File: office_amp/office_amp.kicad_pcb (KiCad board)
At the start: 4 copper layers, 120 x 100 mm, 88 parts, among them J1 Jack-DC, J2 Conn_01x03_Female, J3 Conn_01x02_Female, J4 Conn_01x02_Female, J5 Conn_01x02_Female, J6 Conn_01x02_Female, J7 Screw_Terminal_01x04, K1 EC2-24NU, K2 EC2-24NU, K3 EC2-24NU, K4 EC2-24NU, Q1 DMT6012LSS, Q2 BC858, Q3 BC858, SW1 SW_SP3T, U1 LM74700, U2 TBA_2-2421, U3 OPA1678, U4 TBA_2-2421, U5 MH-M18, U6 TPA3123D2, U7 OPA1678, U8 IL300, U9 IL300

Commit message: zwischenstand
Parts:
- removed JP3, JP4: Jumper_2_Open, Jumper:SolderJumper-2_P1.3mm_Open_TrianglePad1.0x1.5mm
- added J8: Conn_01x03_Female, Connector_PinHeader_2.54mm:PinHeader_1x03_P2.54mm_Vertical, F.Cu at (174.0, 48.3)
- moved D1 258.2 mm to (203.0, 40.0)
- moved C29 253.8 mm to (203.5, 77.1), turned to 270 degrees
- moved C26 252.9 mm to (202.4, 83.1), turned to 0 degrees
- moved C27 250.9 mm to (202.4, 71.0), turned to 0 degrees
- moved R5 245.1 mm to (198.5, 83.1), turned to 0 degrees
- moved R6 243.1 mm to (198.5, 71.0), turned to 0 degrees
- moved U3 242.8 mm to (198.0, 77.1), turned to 90 degrees
- moved K4 242.3 mm to (180.3, 43.2)
- moved D4 237.3 mm to (193.0, 40.0)
- moved C30 236.0 mm to (194.0, 82.2), turned to 270 degrees
- moved K1 235.4 mm to (200.7, 43.2)
- moved K2 234.5 mm to (190.5, 43.2)
- moved C31 234.2 mm to (194.0, 72.0), turned to 270 degrees
- moved D6 233.0 mm to (182.9, 40.0)
- moved R7 232.0 mm to (192.0, 82.2), turned to 270 degrees
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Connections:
- C28 pad 2: GND_BT -> GND_Input
- C29 pad 1: GND_BT -> GND_Input
- C6 pad 2: PGND -> GNDREF
- C7 pad 2: GND_BT -> GND_Input
- C9 pad 1: GND_BT -> GND_Input
- D1 pad 1: V+ -> Net-(D1-Pad1)
- D1 pad 2: Net-(D1-Pad2) -> GNDREF
- D4 pad 1: V+ -> Net-(D1-Pad1)
- D4 pad 2: Net-(D4-Pad2) -> GNDREF
- D5 pad 1: V+ -> Net-(D5-Pad1)
- D5 pad 2: Net-(D5-Pad2) -> GNDREF
- D6 pad 1: V+ -> Net-(D5-Pad1)
- D6 pad 2: Net-(D6-Pad2) -> GNDREF
- J2 pad 1: (no net) -> GND_An_In
- K1 pad 1: Net-(K1-Pad1) -> Net-(D1-Pad1)
- K1 pad 10: (no net) -> L-In-USB
- K1 pad 12: Net-(D1-Pad2) -> GNDREF
- K1 pad 3: (no net) -> R-In-USB
- K2 pad 1: Net-(K1-Pad1) -> Net-(D1-Pad1)
- K2 pad 12: Net-(D4-Pad2) -> GNDREF
- K2 pad 4: GND_BT -> GND_Input
- K3 pad 1: Net-(K3-Pad1) -> Net-(D5-Pad1)
- K3 pad 12: Net-(D5-Pad2) -> GNDREF
- K4 pad 1: Net-(K3-Pad1) -> Net-(D5-Pad1)
- K4 pad 12: Net-(D6-Pad2) -> GNDREF
- Q2 pad 3: GND_BT -> GND_Input
- Q3 pad 3: GND_BT -> GND_Input
- SW1 pad 2: Net-(K1-Pad1) -> Net-(D1-Pad1)
- SW1 pad 4: Net-(K3-Pad1) -> Net-(D5-Pad1)
- U3 pad 3: GND_BT -> GND_Input
- U3 pad 5: GND_BT -> GND_Input
- U4 pad 2: PGND -> GNDREF
- U4 pad 5: GND_BT -> GND_Input
- U8 pad 4: GND_BT -> GND_Input
- U9 pad 4: GND_BT -> GND_Input
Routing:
- net GNDREF: track 0.00 -> 510.5 mm, vias 0 -> 7
- net V+: track 0.00 -> 301.5 mm, vias 0 -> 25
- net Net-(D1-Pad1): track 0.00 -> 71.3 mm
- net GND_Input: track 0.00 -> 67.1 mm
- net +5VA: track 0.00 -> 63.1 mm
- net /Power/Vin: track 0.00 -> 59.6 mm
- net Net-(D5-Pad1): track 0.00 -> 57.5 mm
- net /Class_D/MUTE: track 0.00 -> 47.7 mm, vias 0 -> 1
- net /Class_D/GAIN0: track 0.00 -> 41.1 mm, vias 0 -> 1
- net /Class_D/~SD: track 0.00 -> 40.0 mm, vias 0 -> 1
- net /Class_D/GAIN1: track 0.00 -> 35.2 mm, vias 0 -> 1
- net /Class_D/ROUT: track 0.00 -> 17.9 mm
- net /Class_D/LOUT: track 0.00 -> 17.9 mm
- net Net-(C22-Pad1): track 0.00 -> 12.9 mm
- net Net-(C23-Pad2): track 0.00 -> 12.9 mm
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- added copper zone on F.Cu, net /Power/Vin
- added copper zone on F.Cu, net V+

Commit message: Change Components
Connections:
- net /Class_D/~SD renamed /Class_D/~{SD}
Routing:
- net Net-(Q1-PadG): track 11.5 -> 12.4 mm
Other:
- net class Default removed
- net class HighPower removed
- net class Power removed

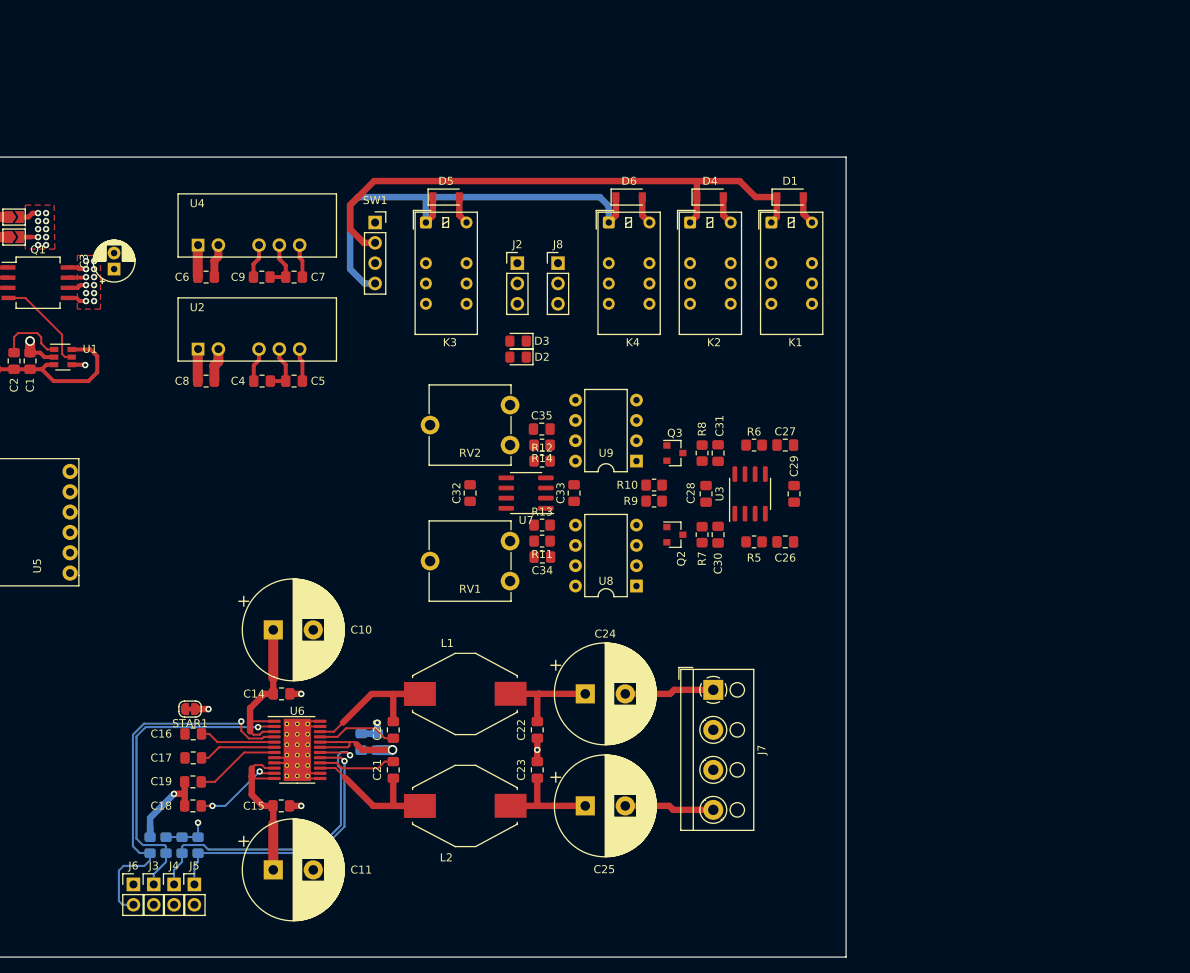
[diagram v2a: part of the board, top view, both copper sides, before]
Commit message: Changed Components to available parts
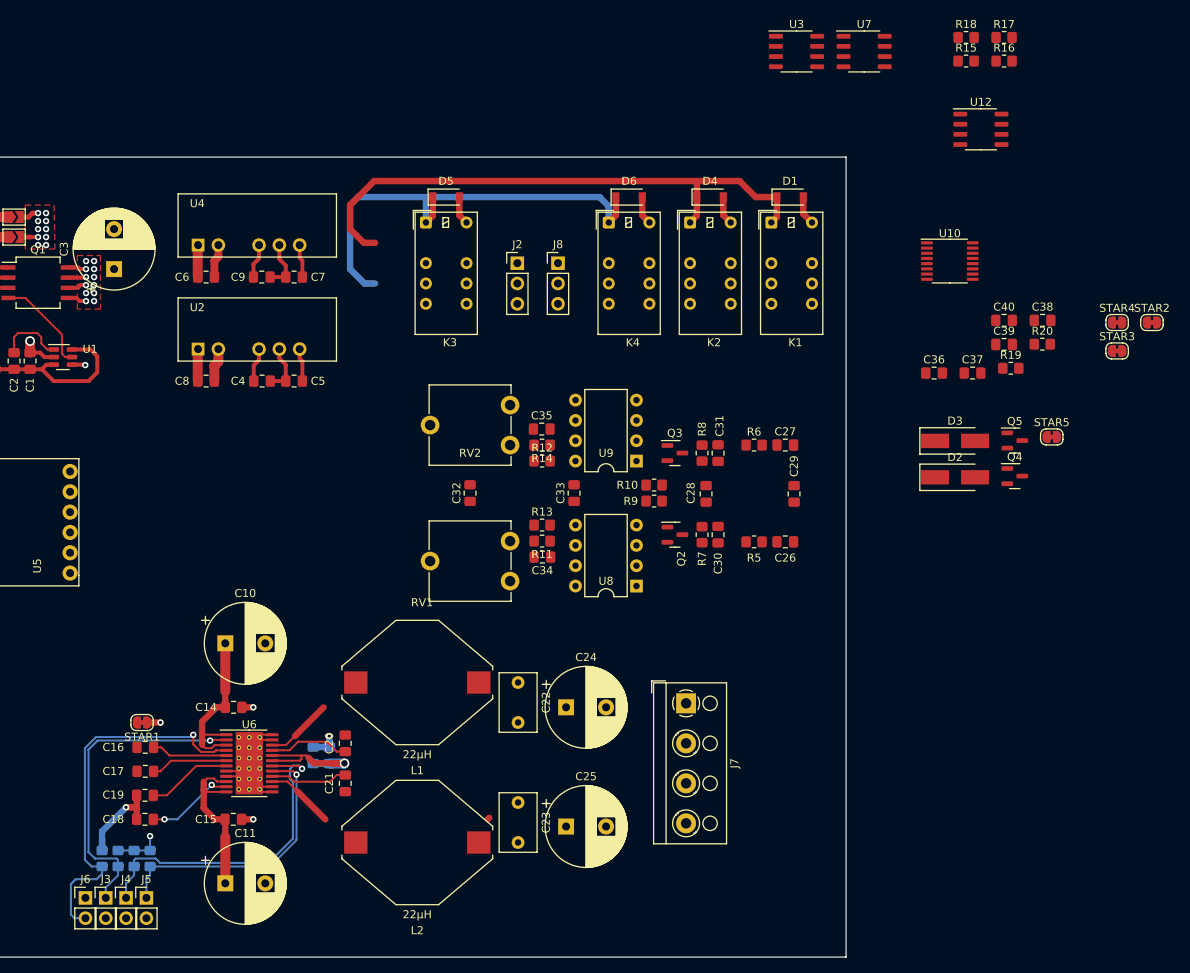
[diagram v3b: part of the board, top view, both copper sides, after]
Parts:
- removed SW1: SW_SP3T, Connector_PinSocket_2.54mm:PinSocket_1x04_P2.54mm_Vertical
- added C36: 100nF, Capacitor_SMD:C_0805_2012Metric_Pad1.18x1.45mm_HandSolder, F.Cu at (221.0, 62.0)
- added C37: 100nF, Capacitor_SMD:C_0805_2012Metric_Pad1.18x1.45mm_HandSolder, F.Cu at (225.8, 62.0)
- added C38: 100nF, Capacitor_SMD:C_0805_2012Metric_Pad1.18x1.45mm_HandSolder, F.Cu at (234.6, 55.4)
- added C39: 100nF, Capacitor_SMD:C_0805_2012Metric_Pad1.18x1.45mm_HandSolder, F.Cu at (229.8, 58.4)
- added C40: 100nF, Capacitor_SMD:C_0805_2012Metric_Pad1.18x1.45mm_HandSolder, F.Cu at (229.8, 55.4)
- added Q4: BC850, Package_TO_SOT_SMD:SOT-23, F.Cu at (231.1, 74.9)
- added Q5: BC850, Package_TO_SOT_SMD:SOT-23, F.Cu at (231.1, 70.4)
- added R15: R, Resistor_SMD:R_0805_2012Metric_Pad1.20x1.40mm_HandSolder, F.Cu at (225.0, 23.0)
- added R16: R, Resistor_SMD:R_0805_2012Metric_Pad1.20x1.40mm_HandSolder, F.Cu at (229.8, 23.0)
- added R17: R, Resistor_SMD:R_0805_2012Metric_Pad1.20x1.40mm_HandSolder, F.Cu at (229.8, 20.1)
- added R18: R, Resistor_SMD:R_0805_2012Metric_Pad1.20x1.40mm_HandSolder, F.Cu at (225.0, 20.1)
- added R19: 4k7, Resistor_SMD:R_0805_2012Metric_Pad1.20x1.40mm_HandSolder, F.Cu at (230.6, 61.4)
- added R20: 4k7, Resistor_SMD:R_0805_2012Metric_Pad1.20x1.40mm_HandSolder, F.Cu at (234.5, 58.4)
- added STAR2: SolderJumper_2_Bridged, Jumper:SolderJumper-2_P1.3mm_Bridged_RoundedPad1.0x1.5mm, F.Cu at (248.2, 55.7)
- added STAR3: SolderJumper_2_Bridged, Jumper:SolderJumper-2_P1.3mm_Bridged_RoundedPad1.0x1.5mm, F.Cu at (243.9, 59.2)
- added STAR4: SolderJumper_2_Bridged, Jumper:SolderJumper-2_P1.3mm_Bridged_RoundedPad1.0x1.5mm, F.Cu at (243.9, 55.7)
- added STAR5: SolderJumper_2_Bridged, Jumper:SolderJumper-2_P1.3mm_Bridged_RoundedPad1.0x1.5mm, F.Cu at (235.7, 70.0)
- added U10: DS1882E, Package_SO:TSSOP-16_4.4x5mm_P0.65mm, F.Cu at (223.0, 48.0)
- added U12: TL082, Package_SO:SO-8_3.9x4.9mm_P1.27mm, F.Cu at (226.8, 31.5)
- C10, C11, C24, C25: footprint Capacitor_THT:CP_Radial_D12.5mm_P5.00mm -> Capacitor_THT:CP_Radial_D10.0mm_P5.00mm
- C16, C17: value 1µF -> 2µ2F
- C22, C23: footprint Capacitor_SMD:C_0805_2012Metric_Pad1.18x1.45mm_HandSolder -> Capacitor_THT:C_Rect_L7.2mm_W4.5mm_P5.00mm_FKS2_FKP2_MKS2_MKP2
- C3: value 47µF -> 470µF; footprint Capacitor_THT:CP_Radial_D5.0mm_P2.00mm -> Capacitor_THT:CP_Radial_D10.0mm_P5.00mm
- D2, D3: value WE 82350120101 -> WE 824500700; footprint Diode_SMD:D_0805_2012Metric_Pad1.15x1.40mm_HandSolder -> Diode_SMD:D_SMA_Handsoldering
- L1, L2: footprint Inductor_SMD:L_Fastron_PISN_Handsoldering -> office_amp:L_Bourns-PM5022
- U3, U7: value OPA1678 -> TL082; footprint Package_SO:SOIC-8_3.9x4.9mm_P1.27mm -> Package_SO:SO-8_3.9x4.9mm_P1.27mm
- moved U7 69.5 mm to (212.3, 21.8), turned to 0 degrees
- moved D2 56.7 mm to (223.6, 75.0), turned to 0 degrees
- moved D3 56.0 mm to (223.6, 70.5), turned to 0 degrees
- moved U3 55.6 mm to (203.8, 21.8), turned to 0 degrees
- moved L2 7.55 mm to (156.4, 120.7)
- moved C22 6.39 mm to (169.0, 100.7)
- moved C18 6.23 mm to (122.4, 117.8)
- moved C19 6.23 mm to (122.4, 114.8)
- moved C10 6.23 mm to (132.4, 95.8)
- moved C11 6.23 mm to (132.4, 125.8)
- moved C12 6.23 mm to (145.4, 109.8)
- moved C13 6.23 mm to (143.4, 109.8)
- moved C14 6.23 mm to (133.4, 103.8)
- moved C15 6.23 mm to (133.4, 117.8)
- moved C16 6.23 mm to (122.4, 108.8)
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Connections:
- C16 pad 1: /Class_D/LIN -> /Class_D/RIN
- C16 pad 2: L-In -> Net-(C16-Pad2)
- C17 pad 1: /Class_D/RIN -> /Class_D/LIN
- C17 pad 2: R-In -> Net-(U12-Pad2)
- C4 pad 1: GNDA -> Net-(C4-Pad1)
- C5 pad 2: GNDA -> Net-(C4-Pad1)
- D1 pad 1: Net-(D1-Pad1) -> V+
- D1 pad 2: GNDREF -> Net-(D1-Pad2)
- D4 pad 1: Net-(D1-Pad1) -> V+
- D4 pad 2: GNDREF -> Net-(D1-Pad2)
- D5 pad 1: Net-(D5-Pad1) -> V+
- D5 pad 2: GNDREF -> Net-(D6-Pad2)
- D6 pad 1: Net-(D5-Pad1) -> V+
- D6 pad 2: GNDREF -> Net-(D6-Pad2)
- K1 pad 1: Net-(D1-Pad1) -> V+
- K1 pad 12: GNDREF -> Net-(D1-Pad2)
- K2 pad 1: Net-(D1-Pad1) -> V+
- K2 pad 10: (no net) -> unconnected-(K2-Pad10)
- K2 pad 12: GNDREF -> Net-(D1-Pad2)
- K2 pad 8: (no net) -> unconnected-(K2-Pad8)
- K2 pad 9: (no net) -> unconnected-(K2-Pad9)
- K3 pad 1: Net-(D5-Pad1) -> V+
- K3 pad 10: (no net) -> unconnected-(K3-Pad10)
- K3 pad 12: GNDREF -> Net-(D6-Pad2)
- K3 pad 3: (no net) -> unconnected-(K3-Pad3)
- K3 pad 8: GNDA -> GND1
- K4 pad 1: Net-(D5-Pad1) -> V+
- K4 pad 12: GNDREF -> Net-(D6-Pad2)
- U2 pad 5: GNDA -> Net-(C4-Pad1)
- U3 pad 2: Net-(C30-Pad2) -> GND_Input
- U3 pad 3: GND_Input -> Net-(C30-Pad2)
- U3 pad 5: GND_Input -> Net-(C31-Pad2)
- U3 pad 6: Net-(C31-Pad2) -> GND_Input
- U5 pad 5: (no net) -> BT-MUTE
- U5 pad 6: (no net) -> BT-KEY
- U7 pad 2: Net-(C34-Pad2) -> GNDA
- U7 pad 3: GNDA -> Net-(C34-Pad2)
- U7 pad 5: GNDA -> Net-(C35-Pad2)
- U7 pad 6: Net-(C35-Pad2) -> GNDA
- U8 pad 7: (no net) -> unconnected-(U8-Pad7)
- U8 pad 8: (no net) -> unconnected-(U8-Pad8)
- U9 pad 7: (no net) -> unconnected-(U9-Pad7)
- U9 pad 8: (no net) -> unconnected-(U9-Pad8)
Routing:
- net V+: track 301.5 -> 425.4 mm
- net Net-(D1-Pad1): track 71.3 -> 0.00 mm
- net Net-(D5-Pad1): track 57.5 -> 0.00 mm
- net Net-(C22-Pad1): track 12.9 -> 0.00 mm
- net Net-(C23-Pad2): track 12.9 -> 0.28 mm
- net /Class_D/R-Out: track 11.2 -> 0.00 mm
- net /Class_D/L-Out: track 11.2 -> 0.00 mm
- net /Class_D/LOUT: track 17.9 -> 8.38 mm
- net /Class_D/ROUT: track 17.9 -> 8.61 mm
- net Net-(C4-Pad1): track 0.00 -> 6.26 mm
- net GNDA: track 6.26 -> 0.00 mm
- net GNDREF: track 510.5 -> 504.6 mm, vias 7 -> 6
